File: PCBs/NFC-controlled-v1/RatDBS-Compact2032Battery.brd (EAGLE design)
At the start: 25.4 x 19.1 mm, 20 parts

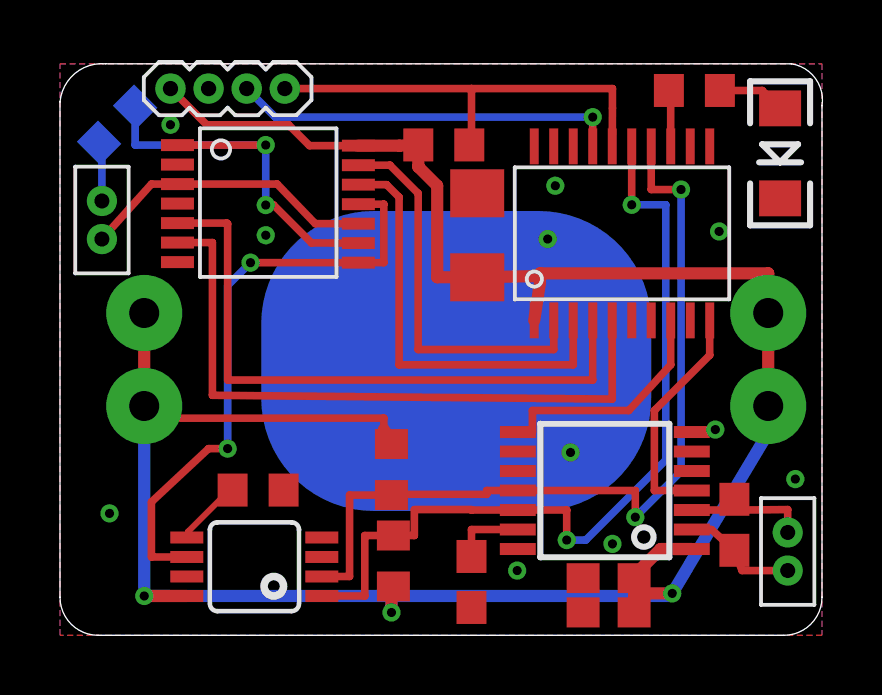
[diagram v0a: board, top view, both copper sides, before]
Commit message: Fixed board errors that were fixed in panelized version
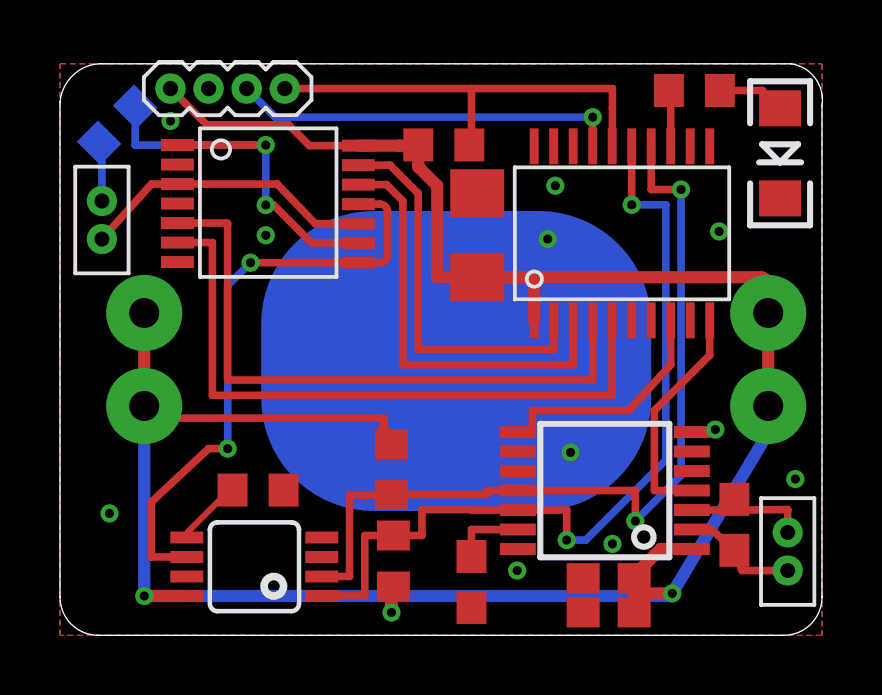
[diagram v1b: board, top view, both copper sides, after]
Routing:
- net VDD: track 82.6 -> 84.0 mm
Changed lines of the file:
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@@
 </class>
 </classes>
-<designrules name="Seeed_DRU">
+<designrules name="Seeed_DRU *">
 <description language="de">&lt;b&gt;EAGLE Design Rules&lt;/b&gt;
 &lt;p&gt;
@@
 <param name="mtCopper" value="0.035mm 0.0175mm 0.035mm 0.035mm 0.035mm 0.035mm 0.035mm 0.035mm 0.035mm 0.035mm 0.035mm 0.035mm 0.035mm 0.035mm 0.0175mm 0.035mm"/>
 <param name="mtIsolate" value="1.5mm 1.1mm 0.2mm 0.15mm 0.2mm 0.15mm 0.2mm 0.15mm 0.2mm 0.15mm 0.2mm 0.15mm 0.2mm 0.15mm 0.2mm"/>
-<param name="mdWireWire" value="6mil"/>
-<param name="mdWirePad" value="6mil"/>
-<param name="mdWireVia" value="6mil"/>
-<param name="mdPadPad" value="6mil"/>
-<param name="mdPadVia" value="6mil"/>
-<param name="mdViaVia" value="6mil"/>
+<param name="mdWireWire" value="8mil"/>
+<param name="mdWirePad" value="8mil"/>
+<param name="mdWireVia" value="8mil"/>
+<param name="mdPadPad" value="8mil"/>
+<param name="mdPadVia" value="8mil"/>
+<param name="mdViaVia" value="8mil"/>
 <param name="mdSmdPad" value="0mil"/>
 <param name="mdSmdVia" value="0mil"/>
@@
 <wire x1="9.652" y1="1.961" x2="9.652" y2="4.6745" width="0.254" layer="1"/>
 <wire x1="11.049" y1="4.6745" x2="9.652" y2="4.6745" width="0.254" layer="1"/>
-<wire x1="20.701" y1="14.859" x2="20.701" y2="5.461" width="0.254" layer="16"/>
-<wire x1="20.701" y1="5.461" x2="19.177" y2="3.937" width="0.254" layer="16"/>
-<wire x1="19.177" y1="3.937" x2="19.177" y2="4.826" width="0.254" layer="1"/>
-<via x="19.177" y="3.937" extent="1-16" drill="0.3048" shape="octagon"/>
+<wire x1="20.701" y1="14.859" x2="20.701" y2="5.334" width="0.254" layer="16"/>
+<wire x1="20.701" y1="5.334" x2="19.177" y2="3.81" width="0.254" layer="16"/>
+<wire x1="19.177" y1="3.81" x2="19.177" y2="4.826" width="0.254" layer="1"/>
+<via x="19.177" y="3.81" extent="1-16" drill="0.3048" shape="octagon"/>
 <wire x1="15.261" y1="4.826" x2="19.177" y2="4.826" width="0.254" layer="1"/>
 <via x="20.701" y="14.859" extent="1-16" drill="0.3048" shape="octagon"/>
@@
 <wire x1="15.261" y1="4.176" x2="13.716" y2="4.176" width="0.254" layer="1"/>
 <wire x1="13.716" y1="4.176" x2="13.716" y2="4.191" width="0.254" layer="1"/>
-<wire x1="13.716" y1="4.191" x2="11.811" y2="4.191" width="0.254" layer="1"/>
-<wire x1="11.811" y1="4.191" x2="11.811" y2="3.3265" width="0.254" layer="1"/>
+<wire x1="13.716" y1="4.191" x2="12.065" y2="4.191" width="0.254" layer="1"/>
+<wire x1="12.065" y1="4.191" x2="12.065" y2="3.3265" width="0.254" layer="1"/>
 <wire x1="19.0575" y1="16.2985" x2="19.0575" y2="14.351" width="0.254" layer="1"/>
 <via x="19.0575" y="14.351" extent="1-16" drill="0.3048" shape="octagon"/>
@@
 <via x="16.891" y="3.175" extent="1-16" drill="0.3048" shape="octagon"/>
 <wire x1="15.261" y1="4.176" x2="16.891" y2="4.176" width="0.254" layer="1"/>
-<wire x1="11.1125" y1="3.3265" x2="11.811" y2="3.3265" width="0.254" layer="1"/>
+<wire x1="11.1125" y1="3.3265" x2="12.065" y2="3.3265" width="0.254" layer="1"/>
 <wire x1="8.727" y1="1.311" x2="10.16" y2="1.311" width="0.254" layer="1"/>
 <wire x1="10.16" y1="1.311" x2="10.16" y2="3.3265" width="0.254" layer="1"/>
@@
 <wire x1="10.795" y1="6.858" x2="10.795" y2="7.239" width="0.254" layer="1"/>
 <wire x1="10.795" y1="7.239" x2="2.808" y2="7.239" width="0.254" layer="1"/>
-<wire x1="15.8076" y1="10.4984" x2="16.002" y2="11.7684" width="0.4064" layer="1"/>
 <contactref element="BAT1" pad="3"/>
 <contactref element="BAT1" pad="4"/>
@@
 <wire x1="23.608" y1="7.644" x2="23.608" y2="6.756" width="0.4064" layer="16"/>
 <wire x1="23.608" y1="6.756" x2="20.408" y2="1.397" width="0.4064" layer="16"/>
-<wire x1="13.9065" y1="11.935" x2="16.002" y2="11.977" width="0.4064" layer="1"/>
-<wire x1="16.002" y1="12.065" x2="16.002" y2="11.977" width="0.4064" layer="1"/>
-<wire x1="16.002" y1="11.977" x2="16.002" y2="11.7684" width="0.4064" layer="1"/>
-<wire x1="23.608" y1="10.744" x2="23.608" y2="12.065" width="0.4064" layer="1"/>
-<wire x1="23.608" y1="12.065" x2="16.002" y2="12.065" width="0.4064" layer="1"/>
 <wire x1="23.608" y1="10.744" x2="23.608" y2="7.644" width="0.4064" layer="1"/>
 <wire x1="3.683" y1="18.2245" x2="4.8895" y2="17.018" width="0.254" layer="1"/>
@@
 <wire x1="11.049" y1="0.762" x2="11.049" y2="1.311" width="0.4064" layer="16"/>
 <via x="11.049" y="0.762" extent="1-16" drill="0.3048" shape="octagon"/>
+<wire x1="13.9065" y1="11.935" x2="15.5536" y2="11.935" width="0.4064" layer="1"/>
+<wire x1="15.5536" y1="11.935" x2="15.8076" y2="11.681" width="0.4064" layer="1" curve="-90"/>
+<wire x1="15.8076" y1="11.681" x2="15.8076" y2="10.4984" width="0.4064" layer="1"/>
+<wire x1="13.9065" y1="11.935" x2="23.354" y2="11.935" width="0.4064" layer="1"/>
+<wire x1="23.354" y1="11.935" x2="23.608" y2="11.681" width="0.4064" layer="1" curve="-90"/>
+<wire x1="23.608" y1="11.681" x2="23.608" y2="10.744" width="0.4064" layer="1"/>
 </signal>
 <signal name="GND">
@@
 <contactref element="LED6" pad="C"/>
 <via x="21.844" y="6.858" extent="1-16" drill="0.3048" shape="octagon"/>
-<via x="3.683" y="17.018" extent="1-16" drill="0.3048" shape="octagon"/>
+<via x="3.683" y="17.145" extent="1-16" drill="0.3048" shape="octagon"/>
 <via x="17.018" y="6.096" extent="1-16" drill="0.3048" shape="octagon"/>
 <via x="18.415" y="3.048" extent="1-16" drill="0.3048" shape="octagon"/>
@@
 <signal name="IN3">
 <contactref element="TS3A4751_0" pad="6"/>
-<wire x1="18.4075" y1="7.874" x2="5.08" y2="8.001" width="0.254" layer="1"/>
+<wire x1="18.4075" y1="8.001" x2="5.08" y2="8.001" width="0.254" layer="1"/>
 <wire x1="3.9155" y1="13.0915" x2="5.08" y2="13.0915" width="0.254" layer="1"/>
 <wire x1="5.08" y1="13.0915" x2="5.08" y2="8.001" width="0.254" layer="1"/>
 <contactref element="MSP430" pad="5"/>
-<wire x1="18.4075" y1="7.874" x2="18.4075" y2="10.4984" width="0.254" layer="1"/>
+<wire x1="18.4075" y1="8.001" x2="18.4075" y2="10.4984" width="0.254" layer="1"/>
 </signal>
 <signal name="IN1">
@@
 <wire x1="3.048" y1="4.445" x2="4.953" y2="6.223" width="0.254" layer="1"/>
 <wire x1="4.953" y1="6.223" x2="5.588" y2="6.223" width="0.254" layer="1"/>
-<wire x1="9.9455" y1="12.4215" x2="10.795" y2="12.4215" width="0.254" layer="1"/>
-<wire x1="10.795" y1="12.4215" x2="10.795" y2="14.3715" width="0.254" layer="1"/>
+<wire x1="9.9455" y1="12.4215" x2="10.668" y2="12.4215" width="0.254" layer="1"/>
+<wire x1="10.668" y1="12.4215" x2="10.922" y2="12.6755" width="0.254" layer="1" curve="90"/>
+<wire x1="10.922" y1="12.6755" x2="10.922" y2="14.1175" width="0.254" layer="1"/>
+<wire x1="10.922" y1="14.1175" x2="10.668" y2="14.3715" width="0.254" layer="1" curve="90"/>
+<wire x1="10.668" y1="14.3715" x2="9.9455" y2="14.3715" width="0.254" layer="1"/>
 <via x="5.588" y="6.223" extent="1-16" drill="0.3048" shape="octagon"/>
-<wire x1="10.795" y1="14.3715" x2="9.9455" y2="14.3715" width="0.254" layer="1"/>
 <wire x1="9.9455" y1="12.4215" x2="6.35" y2="12.4215" width="0.254" layer="1"/>
 <via x="6.35" y="12.4215" extent="1-16" drill="0.3048" shape="octagon"/>
@@
 <contactref element="MSP430" pad="3"/>
 <wire x1="9.9455" y1="15.0215" x2="10.8865" y2="15.0215" width="0.254" layer="1"/>
-<wire x1="10.8865" y1="15.0215" x2="11.303" y2="14.605" width="0.254" layer="1"/>
-<wire x1="11.303" y1="14.605" x2="11.303" y2="9.017" width="0.254" layer="1"/>
-<wire x1="11.303" y1="9.017" x2="17.1075" y2="9.017" width="0.254" layer="1"/>
+<wire x1="10.8865" y1="15.0215" x2="11.43" y2="14.478" width="0.254" layer="1"/>
+<wire x1="11.43" y1="14.478" x2="11.43" y2="9.017" width="0.254" layer="1"/>
+<wire x1="11.43" y1="9.017" x2="17.1075" y2="9.017" width="0.254" layer="1"/>
 <wire x1="17.1075" y1="9.017" x2="17.1075" y2="10.4984" width="0.254" layer="1"/>
 </signal>
